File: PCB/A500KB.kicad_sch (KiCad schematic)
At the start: 251 parts, among them J1 N/A, J2 USB_B_Micro, J3 Conn_02x03_Odd_Even, J4 Conn_01x08_Male, J5 Conn_01x02, J6 N/A, J7 Conn_01x04, Q1 MMBT3904, U1 IS32FL3237_DS, U2 AT90USB1287-A, Y2 16 MHz

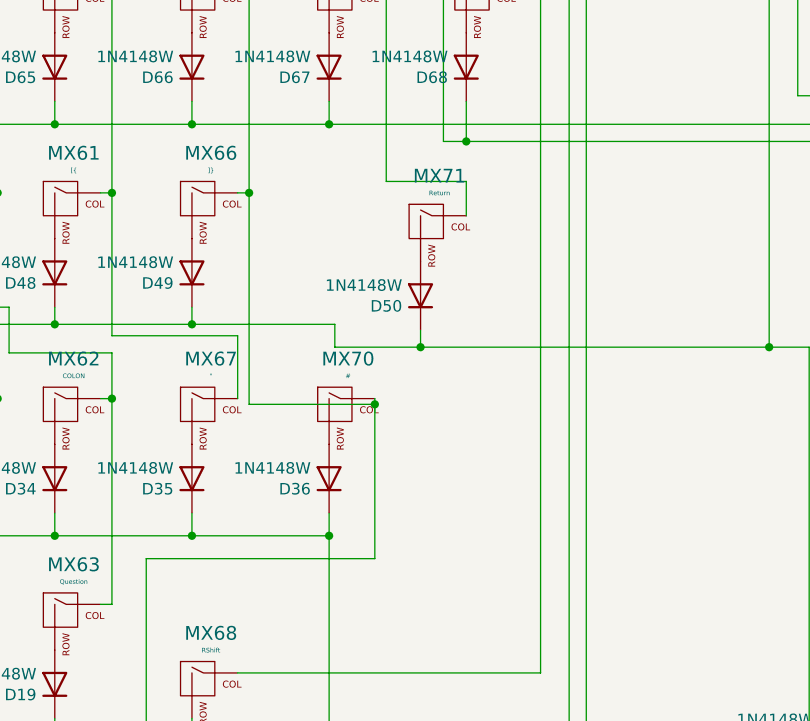
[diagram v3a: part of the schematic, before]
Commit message: added US-Only version (large Return, 2.75U LShift)
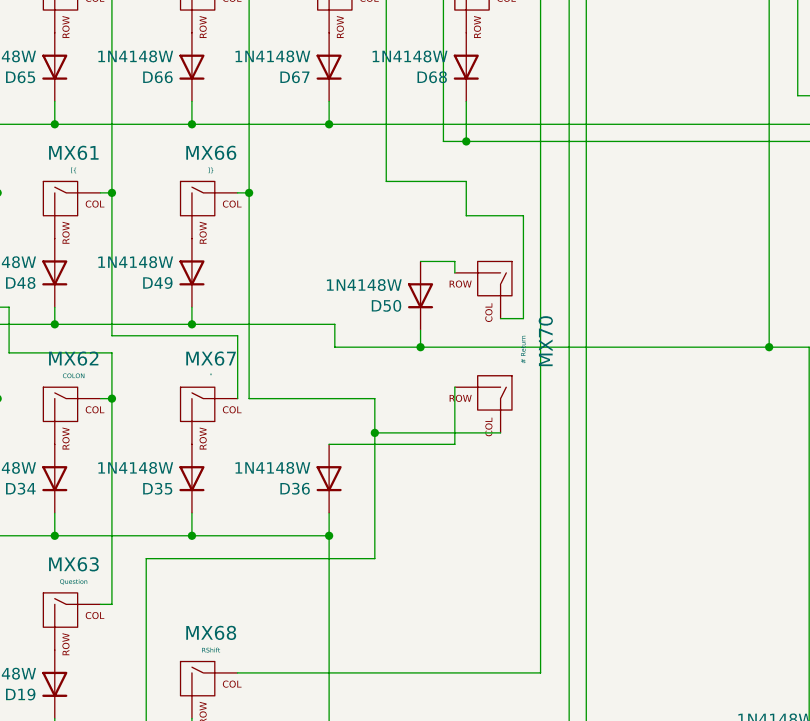
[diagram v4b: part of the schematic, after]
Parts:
- removed MX70: #, MXMitsumi:MXMitsumi-1U-NoLED, symbol MX_Hybrid:MX-NoLED
- removed MX71: Return, MXMitsumi:MXMitsumi-ISO-NoLED, symbol MX_Hybrid:MX-NoLED
- added MX70: # Return, MXMitsumi:MXMitsumi-ISO-Combo-Hash, symbol MX_Hybrid:MX-LSHIFT_LR
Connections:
- net Y1=28: now also MX70.1 (COL)
- net Y2=27: now also MX70.3 (COL)
- net at D36.2 (A): now also MX70.4 (ROW)
- net at D50.2 (A): now also MX70.2 (ROW)
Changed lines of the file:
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@@
 	)
 	(junction
-		(at 256.54 339.725)
-		(diameter 0)
-		(color 0 0 0 0)
-	)
-	(junction
 		(at 138.43 316.23)
 		(diameter 0)
@@
 	)
 	(junction
+		(at 256.54 342.9)
+		(diameter 0)
+		(color 0 0 0 0)
+	)
+	(junction
 		(at 317.5 382.27)
 		(diameter 0)
@@
 	(wire
 		(pts
-			(xy 256.54 339.725) (xy 256.54 356.87)
-		)
-		(stroke
-			(width 0)
-			(type default)
-		)
-	)
-	(wire
-		(pts
 			(xy 118.745 67.31) (xy 121.285 67.31)
 		)
@@
 	(wire
 		(pts
+			(xy 256.54 342.9) (xy 256.54 356.87)
+		)
+		(stroke
+			(width 0)
+			(type default)
+		)
+	)
+	(wire
+		(pts
 			(xy 328.93 367.03) (xy 328.93 360.045)
 		)
@@
 	(wire
 		(pts
+			(xy 273.05 330.2) (xy 270.51 330.2)
+		)
+		(stroke
+			(width 0)
+			(type default)
+		)
+	)
+	(wire
+		(pts
 			(xy 406.4 353.06) (xy 406.4 375.285)
 		)
@@
 	(wire
 		(pts
+			(xy 251.46 344.17) (xy 265.43 344.17)
+		)
+		(stroke
+			(width 0)
+			(type default)
+		)
+	)
+	(wire
+		(pts
 			(xy 101.6 354.33) (xy 116.84 354.33)
 		)
@@
 	(wire
 		(pts
+			(xy 256.54 339.09) (xy 256.54 342.9)
+		)
+		(stroke
+			(width 0)
+			(type default)
+		)
+	)
+	(wire
+		(pts
 			(xy 121.285 128.27) (xy 104.775 128.27)
 		)
@@
 	(wire
 		(pts
-			(xy 200.025 193.675) (xy 217.805 193.675)
+			(xy 265.43 344.17) (xy 265.43 337.82)
 		)
 		(stroke
@@
 	(wire
 		(pts
-			(xy 120.015 40.64) (xy 123.825 40.64)
+			(xy 200.025 193.675) (xy 217.805 193.675)
 		)
 		(stroke
@@
 	(wire
 		(pts
-			(xy 262.255 230.505) (xy 262.255 224.79)
+			(xy 120.015 40.64) (xy 123.825 40.64)
 		)
 		(stroke
@@
 	(wire
 		(pts
-			(xy 256.54 339.09) (xy 256.54 339.725)
+			(xy 262.255 230.505) (xy 262.255 224.79)
 		)
 		(stroke
@@
 	(wire
 		(pts
+			(xy 273.05 318.77) (xy 273.05 330.2)
+		)
+		(stroke
+			(width 0)
+			(type default)
+		)
+	)
+	(wire
+		(pts
 			(xy 543.56 70.485) (xy 550.545 70.485)
 		)
@@
 	(wire
 		(pts
+			(xy 266.7 318.77) (xy 273.05 318.77)
+		)
+		(stroke
+			(width 0)
+			(type default)
+		)
+	)
+	(wire
+		(pts
 			(xy 152.4 240.03) (xy 249.555 240.03)
 		)
@@
 	(wire
 		(pts
+			(xy 261.62 323.85) (xy 265.43 323.85)
+		)
+		(stroke
+			(width 0)
+			(type default)
+		)
+	)
+	(wire
+		(pts
 			(xy 132.08 330.835) (xy 132.08 328.93)
 		)
@@
 	(wire
 		(pts
+			(xy 265.43 323.85) (xy 265.43 325.12)
+		)
+		(stroke
+			(width 0)
+			(type default)
+		)
+	)
+	(wire
+		(pts
 			(xy 508 146.685) (xy 508 142.875)
 		)
@@
 	(wire
 		(pts
-			(xy 242.57 339.725) (xy 256.54 339.725)
-		)
-		(stroke
-			(width 0)
-			(type default)
-		)
-	)
-	(wire
-		(pts
 			(xy 360.045 230.505) (xy 262.255 230.505)
 		)
@@
 	(wire
 		(pts
+			(xy 256.54 339.09) (xy 242.57 339.09)
+		)
+		(stroke
+			(width 0)
+			(type default)
+		)
+	)
+	(wire
+		(pts
 			(xy 227.33 24.765) (xy 227.33 33.655)
 		)
@@
 	(wire
 		(pts
+			(xy 256.54 342.9) (xy 270.51 342.9)
+		)
+		(stroke
+			(width 0)
+			(type default)
+		)
+	)
+	(wire
+		(pts
 			(xy 332.74 183.515) (xy 335.28 183.515)
 		)
@@
 	(wire
 		(pts
-			(xy 242.57 316.23) (xy 242.57 339.725)
+			(xy 242.57 316.23) (xy 242.57 339.09)
 		)
 		(stroke
@@
 	(symbol
 		(lib_id "MX_Hybrid:MX-NoLED")
-		(at 252.73 340.36 0)
-		(unit 1)
-		(exclude_from_sim no)
-		(in_bom yes)
-		(on_board yes)
-		(dnp no)
-		(property "Reference" "MX70"
-			(at 253.5682 334.6958 0)
-			(effects
-				(font
-					(size 1.524 1.524)
-				)
-			)
-		)
-		(property "Value" "#"
-			(at 253.5682 336.5754 0)
-			(effects
-				(font
-					(size 0.508 0.508)
-				)
-			)
-		)
-		(property "Footprint" "MXMitsumi:MXMitsumi-1U-NoLED"
-			(at 236.855 340.995 0)
-			(effects
-				(font
-					(size 1.524 1.524)
-				)
-				(hide yes)
-			)
-		)
-		(property "Datasheet" ""
-			(at 236.855 340.995 0)
-			(effects
-				(font
-					(size 1.524 1.524)
-				)
-				(hide yes)
-			)
-		)
-		(property "Description" ""
-			(at 252.73 340.36 0)
-			(effects
-				(font
-					(size 1.27 1.27)
-				)
-				(hide yes)
-			)
-		)
-		(pin "1"
-		)
-		(pin "2"
-		)
-		(instances
-			(project ""
-				(path "/0fb41543-9ec7-44b0-8d09-79a8fb596336"
-					(reference "MX70")
-					(unit 1)
-				)
-			)
-		)
-	)
-	(symbol
-		(lib_id "MX_Hybrid:MX-NoLED")
 		(at 87.63 362.585 0)
 		(unit 1)
@@
 	(symbol
 		(lib_id "MX_Hybrid:MX-NoLED")
-		(at 262.89 320.04 0)
-		(unit 1)
-		(exclude_from_sim no)
-		(in_bom yes)
-		(on_board yes)
-		(dnp no)
-		(property "Reference" "MX71"
-			(at 263.7282 314.3758 0)
-			(effects
-				(font
-					(size 1.524 1.524)
-				)
-			)
-		)
-		(property "Value" "Return"
-			(at 263.7282 316.2554 0)
-			(effects
-				(font
-					(size 0.508 0.508)
-				)
-			)
-		)
-		(property "Footprint" "MXMitsumi:MXMitsumi-ISO-NoLED"
-			(at 247.015 320.675 0)
-			(effects
-				(font
-					(size 1.524 1.524)
-				)
-				(hide yes)
-			)
-		)
-		(property "Datasheet" ""
-			(at 247.015 320.675 0)
-			(effects
-				(font
-					(size 1.524 1.524)
-				)
-				(hide yes)
-			)
-		)
-		(property "Description" ""
-			(at 262.89 320.04 0)
-			(effects
-				(font
-					(size 1.27 1.27)
-				)
-				(hide yes)
-			)
-		)
-		(pin "1"
-		)
-		(pin "2"
-		)
-		(instances
-			(project ""
-				(path "/0fb41543-9ec7-44b0-8d09-79a8fb596336"
-					(reference "MX71")
-					(unit 1)
-				)
-			)
-		)
-	)
-	(symbol
-		(lib_id "MX_Hybrid:MX-NoLED")
 		(at 307.975 299.72 0)
 		(unit 1)
@@
 					(unit 1)
 				)
+			)
+		)
+	)
+	(symbol
+		(lib_id "MX_Hybrid:MX-LSHIFT_LR")
+		(at 269.24 326.39 270)
+		(unit 1)
+		(exclude_from_sim no)
+		(in_bom yes)
+		(on_board yes)
+		(dnp no)
+		(property "Reference" "MX70"
+			(at 275.59 332.74 0)
+			(effects
+				(font
+					(size 1.524 1.524)
+				)
+			)
+		)
+		(property "Value" "# Return"
+			(at 273.05 333.6352 0)
+			(effects
+				(font
+					(size 0.508 0.508)
+				)
+			)
+		)
+		(property "Footprint" "MXMitsumi:MXMitsumi-ISO-Combo-Hash"
+			(at 268.605 310.515 0)
+			(effects
+				(font
+					(size 1.524 1.524)
+				)
+				(hide yes)
+			)
+		)
+		(property "Datasheet" ""
+			(at 268.605 310.515 0)
+			(effects
+				(font
+					(size 1.524 1.524)
+				)
+				(hide yes)
+			)
+		)
+		(property "Description" ""
+			(at 269.24 326.39 0)
+			(effects
+				(font
+					(size 1.27 1.27)
+				)
+				(hide yes)
+			)
+		)
+		(pin "4"
+		)
+		(pin "3"
+		)
+		(pin "2"
+		)
+		(pin "1"
+		)
+		(instances
+			(project "A500KB"
+				(path "/0fb41543-9ec7-44b0-8d09-79a8fb596336"
+					(reference "MX70")
+					(unit 1)
+				)
